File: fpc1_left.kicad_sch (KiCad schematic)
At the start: 6 parts, among them J2430 left power loom, straight-num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, J2441 main ground strap, J2443 main ground strap

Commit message: work on the power redesign and case
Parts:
- added J2450: left power rails, ducktop2:WAGO_2060_453_SMD, symbol Connector_Generic:Conn_01x03
- added J2460: left power return, ducktop2:WAGO_2060_451_SMD, symbol Connector_Generic:Conn_01x01
- J2430: value left power loom, straight-numbered -> left power rails; footprint Connector_Molex:Molex_Micro-Fit_3.0_43045-1212_2x06_P3.00mm_Vertical -> ducktop2:WAGO_2060_453_SMD; symbol Connector_Generic:Conn_02x06_Odd_Even -> Connector_Generic:Conn_01x03; Assembly (none) -> strip 7..9 mm; hold the button to insert or remove stranded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; Contacts 43030-0038 tin 18 AWG -> (none); CurrentRatingBasis PS-43045 R; use 12-circuit 18 AWG 5.5 A reference screen; a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 -> 9 A IEC and UL; the 10 A ground-cut screen requires both se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; HarnessPinOrder pin n to pin n; continuity and isolation test every conduct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 -> match rail names in the harness drawing; each three-pole gr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; HarnessWireLength 90..100 mm between crimp barrels, including tolerance -> (none); MPN 43045-1212 -> 2060-453/998-404; Manufacturer Molex -> WAGO; MatedHeight 17.64 mm connector body; current 90..100 mm wire poses requ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 -> 4.5 mm terminal body; wire and release-tool envelopes are s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; MatingHousing 43025-1200 -> (none); ResistanceAcceptance termination <=45 mOhm hot/aged; wire <=30 mOhm/m hot; each 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 -> (none); ReturnAcceptance (none) -> remaining complete braid <=1 mOhm; each return wire >=0.12 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; Wire Alpha Wire 3253 UL1061 18 AWG tinned stranded -> Alpha 6715, 18 AWG 16/30 tinned copper; no ferrule
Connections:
- net AUX_DC_RAW: now also J2450.3 (Pin_3); no longer J2430.4 (Pin_4)
- net GND: now also J2460.1 (Pin_1); no longer J2430.10 (Pin_10), J2430.11 (Pin_11), J2430.12 (Pin_12), J2430.7 (Pin_7), J2430.8 (Pin_8), J2430.9 (Pin_9)
- net MCU_3V3: now also J2450.1 (Pin_1); no longer J2430.6 (Pin_6)
- net SYS_3V3: now also J2450.2 (Pin_2); no longer J2430.5 (Pin_5)
- net USB_PD_SELECTED: now also J2430.1 (Pin_1); no longer J2430.3 (Pin_3)
- net VSYS: now also J2430.3 (Pin_3); no longer J2430.1 (Pin_1)

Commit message: rework the board placement and fix more power stuff
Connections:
- net PD1_EFUSE_FAULT_N renamed PD1_EFUSE_PG
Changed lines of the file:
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@@
   (effects (font (size 1.27 1.27)) (justify right bottom))
 )
-(hierarchical_label "PD1_EFUSE_FAULT_N"
+(hierarchical_label "PD1_EFUSE_PG"
   (shape bidirectional)
   (at 54.61 322.58 180)

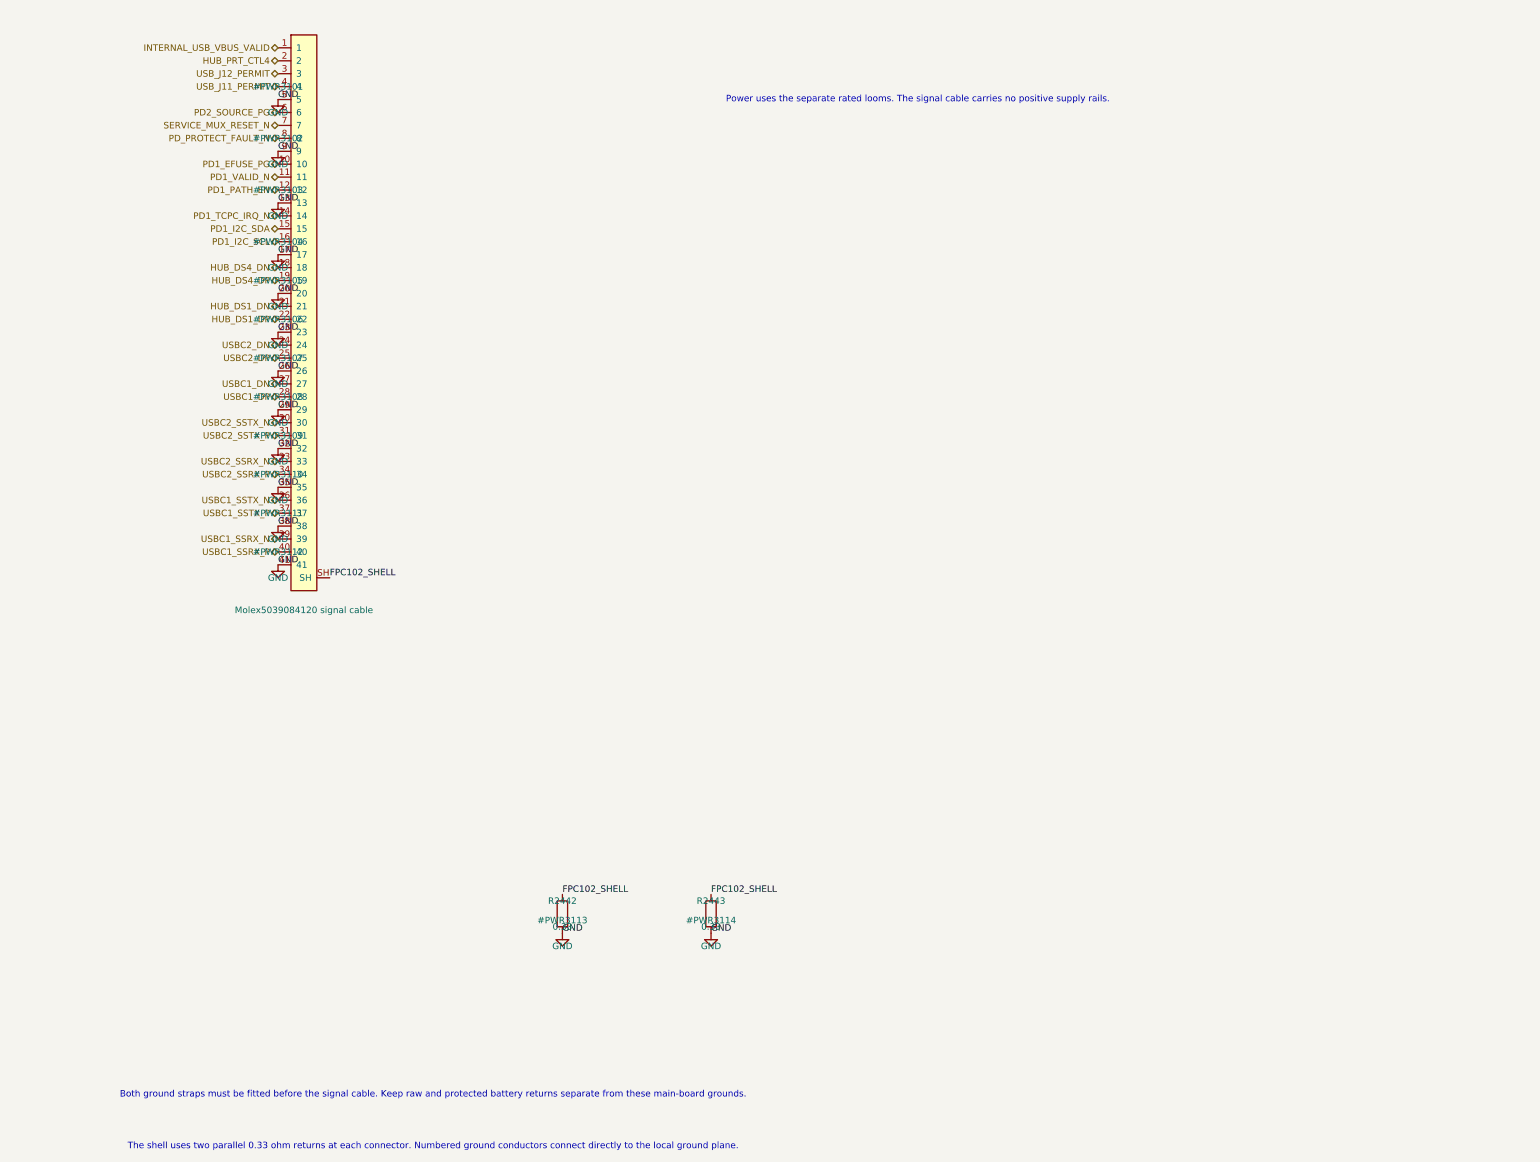
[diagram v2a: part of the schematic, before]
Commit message: finish the new bms and move the connectors up top
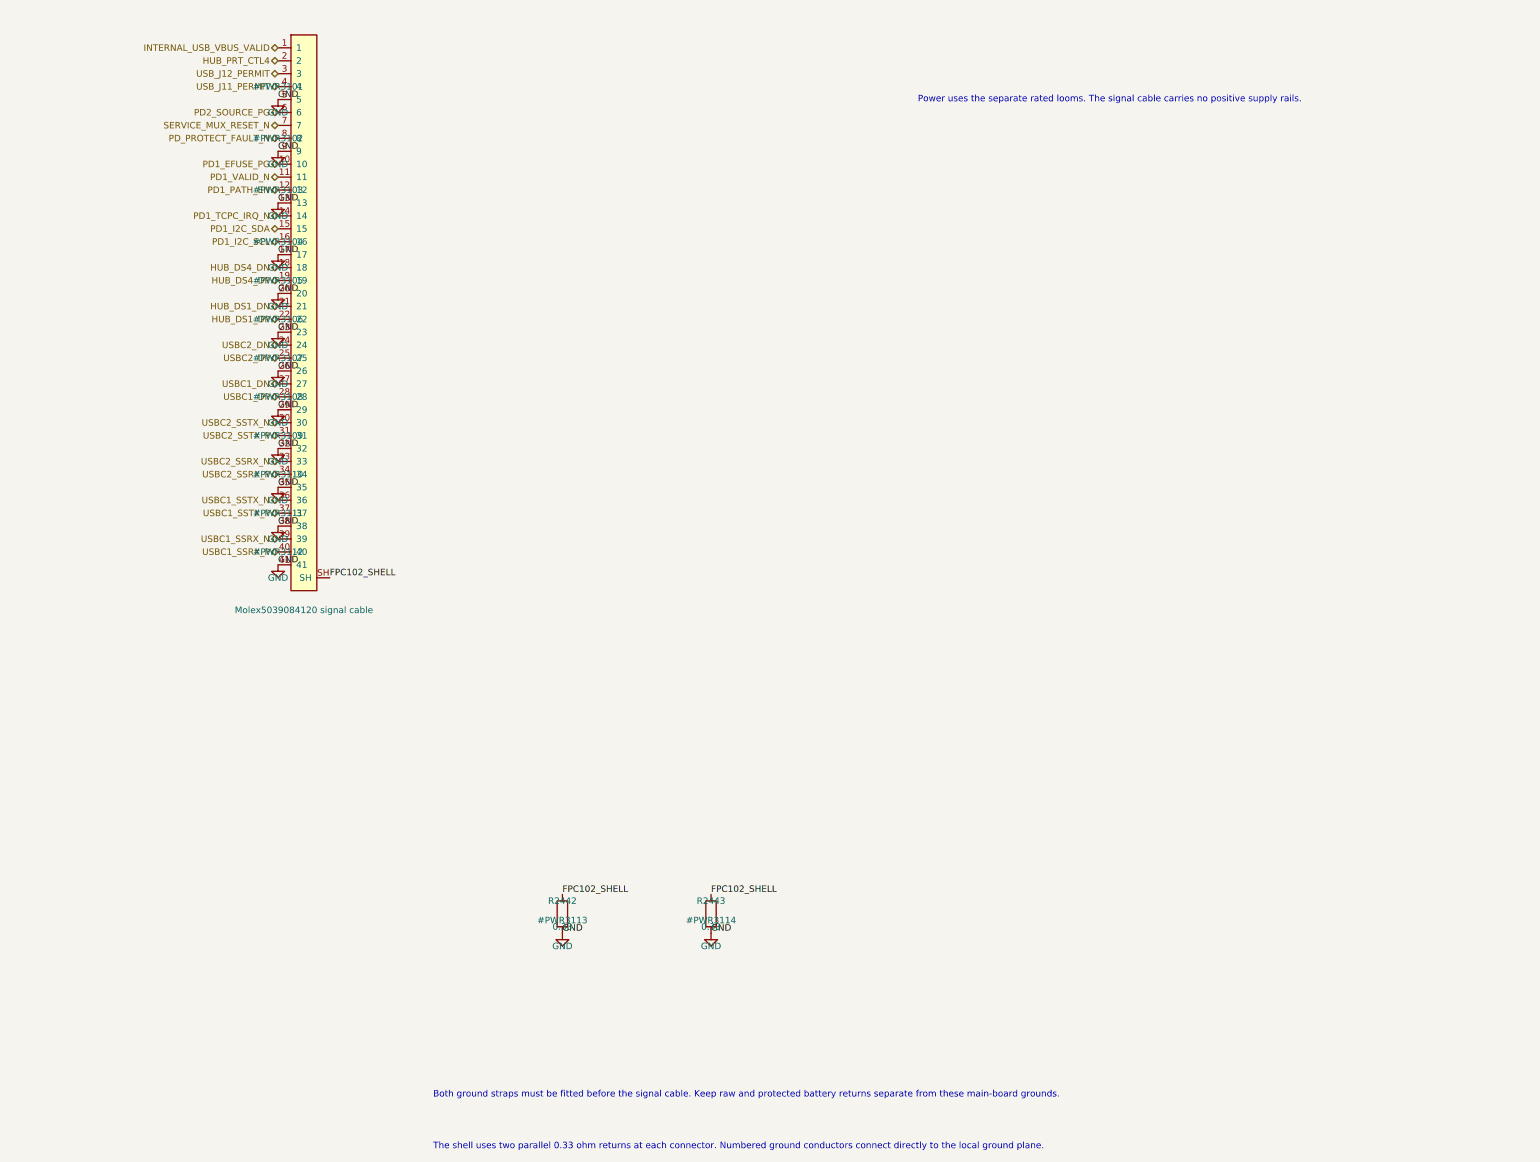
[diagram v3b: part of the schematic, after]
